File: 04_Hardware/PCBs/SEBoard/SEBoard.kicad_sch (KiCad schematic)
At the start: 0 parts

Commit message: feat(schematic): add SE250B4 symbol to schematic (unchecked)
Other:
- note added: "1.8V/?mA"
- note added: "2.96V/?mA"
- note added: "3V/?mA"
- note added: "CAM0_1V1_EN"
- note added: "LCM_VCC_EN"
- note added: "SE250B4"
- note added: "VREG_L15A_1P8_AB49"
- note added: "VREG_L17A_3P0"
- note added: "VREG_L20A_2P96"
- note added: "[2.96 V output power for Camera AVDD & AF-VDD]"
- note removed: "1.8V/200mA"
- note removed: "1.8V/300mA"
- note removed: "2.8V/500mA"
- note removed: "3V/192mA"
- note removed: "GPIO_104"
- note removed: "GPIO_106"
- note removed: "SC200E"
- note removed: "[2.8 V output power for Camera AVDD & AF-VDD]"
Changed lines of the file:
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@@
 	(title_block
 		(title "Block Diagram")
-		(date "2024-06-09")
+		(date "2026-04-26")
 		(rev "v1.0")
 		(company "Author: Mehmet Cihangir")
@@
 		)
 	)
+	(text "VREG_L15A_1P8_AB49"
+		(exclude_from_sim no)
+		(at 141.224 196.088 0)
+		(effects
+			(font
+				(size 1.27 1.27)
+			)
+		)
+	)
 	(text "UARTs"
 		(exclude_from_sim no)
@@
 		)
 	)
-	(text "1.8V/300mA"
-		(exclude_from_sim no)
-		(at 157.48 199.898 0)
+	(text "1.8V/?mA"
+		(exclude_from_sim no)
+		(at 159.004 199.898 0)
 		(effects
 			(font
@@
 		)
 	)
+	(text "VREG_L20A_2P96"
+		(exclude_from_sim no)
+		(at 138.938 203.708 0)
+		(effects
+			(font
+				(size 1.27 1.27)
+			)
+		)
+	)
 	(text "I2C/SPI"
 		(exclude_from_sim no)
@@
 		)
 	)
-	(text "GPIO_104"
-		(exclude_from_sim no)
-		(at 180.34 233.172 0)
+	(text "LCM_VCC_EN"
+		(exclude_from_sim no)
+		(at 179.07 232.918 0)
 		(effects
 			(font
@@
 		)
 	)
-	(text "SC200E"
+	(text "SE250B4"
 		(exclude_from_sim no)
 		(at 173.228 92.71 0)
@@
 		)
 	)
+	(text "VREG_L17A_3P0"
+		(exclude_from_sim no)
+		(at 138.43 207.518 0)
+		(effects
+			(font
+				(size 1.27 1.27)
+			)
+		)
+	)
 	(text "1A @3.8V"
 		(exclude_from_sim no)
@@
 		)
 	)
+	(text "VREG_L15A_1P8_AB49"
+		(exclude_from_sim no)
+		(at 141.224 199.898 0)
+		(effects
+			(font
+				(size 1.27 1.27)
+			)
+		)
+	)
 	(text "eSIM"
 		(exclude_from_sim no)
@@
 		)
 	)
-	(text "2.8V/500mA"
-		(exclude_from_sim no)
-		(at 157.734 203.708 0)
+	(text "2.96V/?mA"
+		(exclude_from_sim no)
+		(at 159.258 203.708 0)
 		(effects
 			(font
@@
 		)
 	)
-	(text "3V/192mA"
-		(exclude_from_sim no)
-		(at 157.734 207.518 0)
+	(text "3V/?mA"
+		(exclude_from_sim no)
+		(at 159.258 207.518 0)
 		(effects
 			(font
@@
 		)
 	)
-	(text "GPIO_106"
-		(exclude_from_sim no)
-		(at 180.34 217.678 0)
+	(text "CAM0_1V1_EN"
+		(exclude_from_sim no)
+		(at 178.562 217.678 0)
 		(effects
 			(font
@@
 		)
 	)
-	(text "1.8V/200mA"
-		(exclude_from_sim no)
-		(at 157.48 196.088 0)
-		(effects
-			(font
-				(size 1.27 1.27)
-			)
-		)
-	)
-	(text "[2.8 V output power for Camera AVDD & AF-VDD]"
+	(text "1.8V/?mA"
+		(exclude_from_sim no)
+		(at 159.004 196.088 0)
+		(effects
+			(font
+				(size 1.27 1.27)
+			)
+		)
+	)
+	(text "[2.96 V output power for Camera AVDD & AF-VDD]"
 		(exclude_from_sim no)
 		(at 202.692 204.724 0)
@@
 		)
 	)
-	(text_box "VBAT"
+	(text_box "VBAT\nVPH_PA"
 		(exclude_from_sim no)
 		(at 110.49 229.87 0)
@@
 		(stroke
 			(width 0)
-			(type default)
+			(type solid)
 		)
 		(fill
@@
 		)
 	)
-	(text_box "SC200E"
+	(text_box "SE250B4"
 		(exclude_from_sim no)
 		(at 110.49 210.82 0)
@@
 		(stroke
 			(width 0)
-			(type default)
-		)
-		(fill
+			(type solid)
+		)
+		(fill

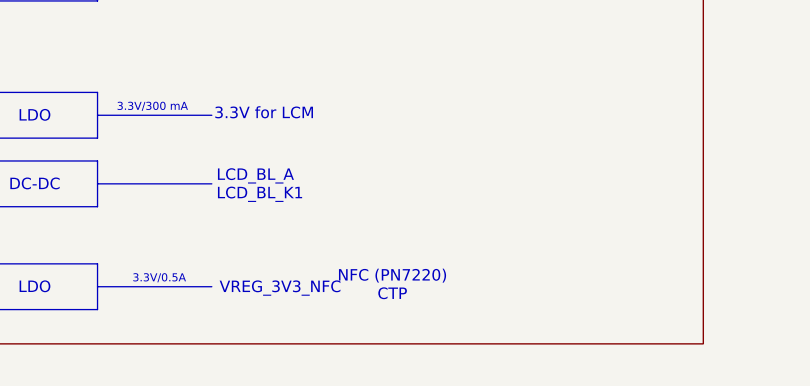
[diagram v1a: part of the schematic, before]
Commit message: feat: Updated schematic layout and moved new components to Layout
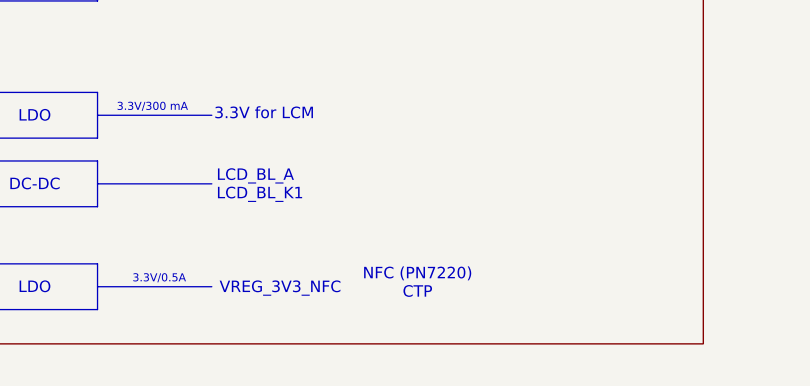
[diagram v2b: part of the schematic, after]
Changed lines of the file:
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@@
 	(text "NFC (PN7220)\nCTP"
 		(exclude_from_sim no)
-		(at 232.156 254 0)
+		(at 234.95 253.746 0)
 		(effects
 			(font
